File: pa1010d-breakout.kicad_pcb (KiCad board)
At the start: 2 copper layers, 19 x 23 mm, 5 parts, among them J1 Conn_01x08_Male, U1 PA1010D

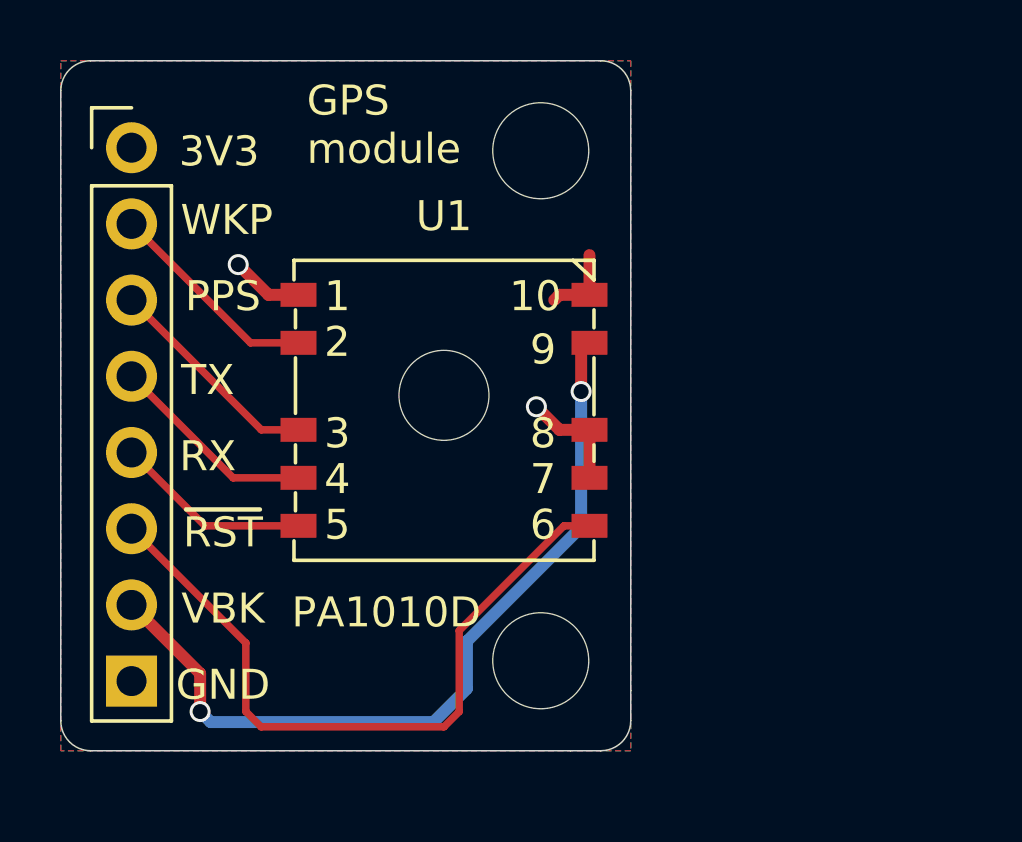
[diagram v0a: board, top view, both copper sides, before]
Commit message: refactor: update schematic according to datasheet V0.3
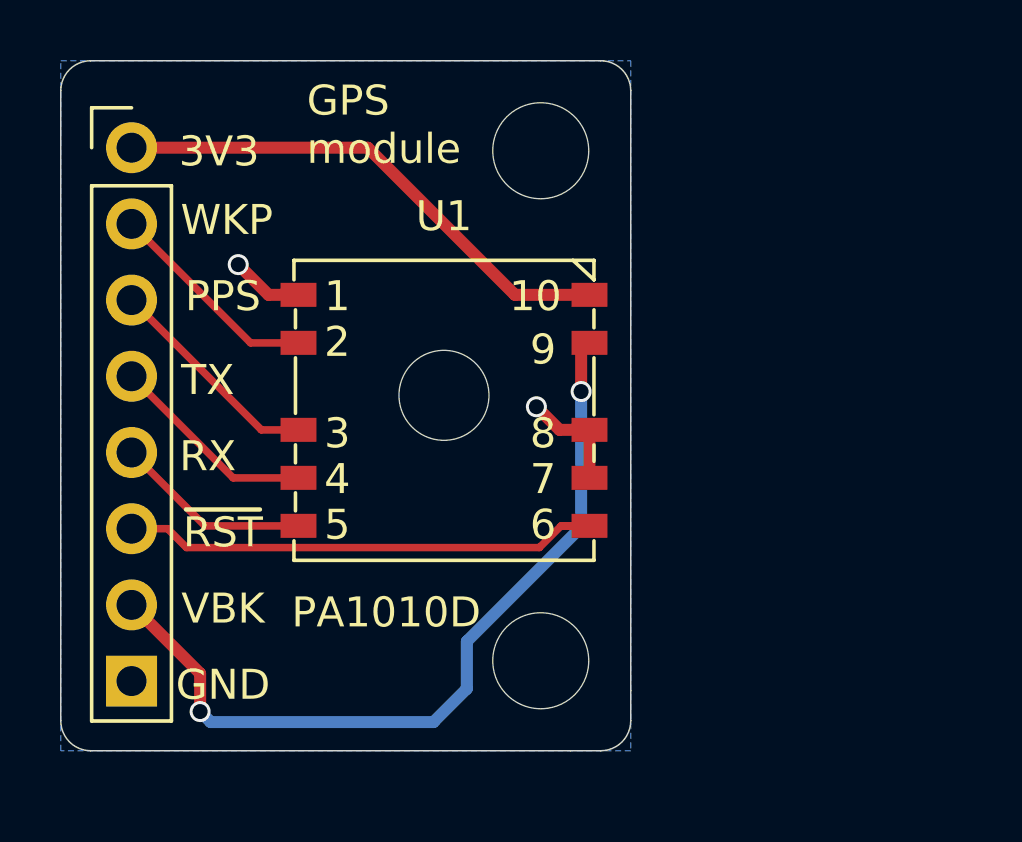
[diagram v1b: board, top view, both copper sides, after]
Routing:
- net +3V3: track 2.57 -> 17.3 mm
- net /NRESET: track 23.7 -> 16.7 mm
- removed copper zone on F.Cu, net +3V3
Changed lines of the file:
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@@
     (thickness 1.6)
     (drawings 52)
-    (tracks 38)
+    (tracks 36)
     (zones 0)
     (modules 5)
@@
   (layers
     (0 F.Cu signal)
-    (31 B.Cu signal)
-    (32 B.Adhes user)
-    (33 F.Adhes user)
-    (34 B.Paste user)
+    (31 B.Cu signal hide)
+    (32 B.Adhes user hide)
+    (33 F.Adhes user hide)
+    (34 B.Paste user hide)
     (35 F.Paste user)
-    (36 B.SilkS user)
+    (36 B.SilkS user hide)
     (37 F.SilkS user)
-    (38 B.Mask user)
+    (38 B.Mask user hide)
     (39 F.Mask user)
-    (40 Dwgs.User user)
-    (41 Cmts.User user)
-    (42 Eco1.User user)
-    (43 Eco2.User user)
+    (40 Dwgs.User user hide)
+    (41 Cmts.User user hide)
+    (42 Eco1.User user hide)
+    (43 Eco2.User user hide)
     (44 Edge.Cuts user)
-    (45 Margin user)
-    (46 B.CrtYd user)
+    (45 Margin user hide)
+    (46 B.CrtYd user hide)
     (47 F.CrtYd user)
-    (48 B.Fab user)
+    (48 B.Fab user hide)
     (49 F.Fab user)
   )
@@
   (segment (start 101.624 82.303) (end 100.624 82.303) (width 0.4) (layer F.Cu) (net 1))
   (via (at 99.855 81.534) (size 0.7) (drill 0.5) (layers F.Cu B.Cu) (net 1))
-  (segment (start 100.624 77.803) (end 100.449 77.978) (width 0.4) (layer F.Cu) (net 2))
-  (segment (start 100.624 77.803) (end 101.624 77.803) (width 0.4) (layer F.Cu) (net 2))
-  (segment (start 101.624 77.803) (end 101.624 76.478) (width 0.4) (layer F.Cu) (net 2))
+  (segment (start 86.36 72.898) (end 94.234 72.898) (width 0.4) (layer F.Cu) (net 2))
+  (segment (start 99.139 77.803) (end 101.624 77.803) (width 0.4) (layer F.Cu) (net 2))
+  (segment (start 94.234 72.898) (end 99.139 77.803) (width 0.4) (layer F.Cu) (net 2))
   (segment (start 86.36 88.138) (end 88.646 90.424) (width 0.4) (layer F.Cu) (net 3))
   (segment (start 88.646 90.424) (end 88.646 91.694) (width 0.4) (layer F.Cu) (net 3))
@@
   (segment (start 97.536 90.932) (end 97.536 89.355998) (width 0.4) (layer B.Cu) (net 3))
   (segment (start 101.346 85.545998) (end 101.346 81.026) (width 0.4) (layer B.Cu) (net 3))
-  (segment (start 97.282 88.995) (end 100.774 85.503) (width 0.25) (layer F.Cu) (net 4))
-  (segment (start 97.282 91.694) (end 97.282 88.995) (width 0.25) (layer F.Cu) (net 4))
   (segment (start 100.774 85.503) (end 101.624 85.503) (width 0.25) (layer F.Cu) (net 4))
-  (segment (start 96.774 92.202) (end 97.282 91.694) (width 0.25) (layer F.Cu) (net 4))
-  (segment (start 90.678 92.202) (end 96.774 92.202) (width 0.25) (layer F.Cu) (net 4))
-  (segment (start 90.17 91.694) (end 90.678 92.202) (width 0.25) (layer F.Cu) (net 4))
-  (segment (start 90.17 89.408) (end 90.17 91.694) (width 0.25) (layer F.Cu) (net 4))
-  (segment (start 86.36 85.598) (end 90.17 89.408) (width 0.25) (layer F.Cu) (net 4))
+  (segment (start 88.192082 86.228001) (end 99.953999 86.228001) (width 0.25) (layer F.Cu) (net 4))
+  (segment (start 87.562081 85.598) (end 88.192082 86.228001) (width 0.25) (layer F.Cu) (net 4))
+  (segment (start 86.36 85.598) (end 87.562081 85.598) (width 0.25) (layer F.Cu) (net 4))
+  (segment (start 100.679 85.503) (end 101.624 85.503) (width 0.25) (layer F.Cu) (net 4))
+  (segment (start 99.953999 86.228001) (end 100.679 85.503) (width 0.25) (layer F.Cu) (net 4))
   (segment (start 88.805 85.503) (end 91.924 85.503) (width 0.25) (layer F.Cu) (net 5))
   (segment (start 86.36 83.058) (end 88.805 85.503) (width 0.25) (layer F.Cu) (net 5))
@@
   (segment (start 90.325 79.403) (end 91.924 79.403) (width 0.25) (layer F.Cu) (net 8))
   (segment (start 86.36 75.438) (end 90.325 79.403) (width 0.25) (layer F.Cu) (net 8))
-  (zone (net 2) (net_name +3V3) (layer F.Cu) (hatch edge 0.508)
-    (connect_pads (clearance 0.508))
-    (min_thickness 0.254)
-    (fill yes (arc_segments 32) (thermal_gap 0.508) (thermal_bridge_width 0.508))
-    (polygon
-      (pts
-        (xy 103 93) (xy 84 93) (xy 84 70) (xy 103 70)
-      )
-    )
-  )
   (zone (net 1) (net_name GND) (layer B.Cu) (hatch edge 0.508)
     (connect_pads (clearance 0.508))

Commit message: refactor: elongate, rotate pads for PA1010D datasheet V0.3
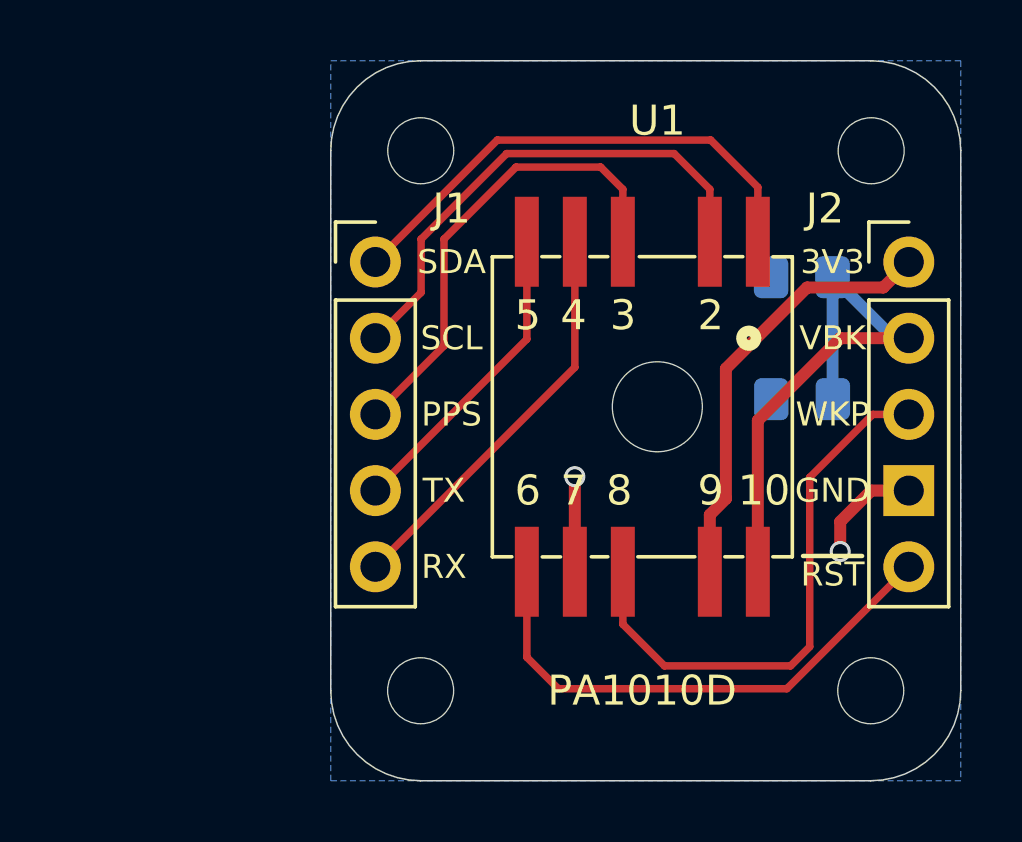
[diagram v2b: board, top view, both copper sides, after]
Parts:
- removed the REF** at (100.0, 73.0)
- removed the REF** at (100.0, 90.0)
- added C1: 0.1uF, Passives:C_0805_2012Metric_Pad1.15x1.40mm_HandSolder, B.Cu at (108.7, 77.2)
- added C2: 1uF, Passives:C_0805_2012Metric_Pad1.15x1.40mm_HandSolder, B.Cu at (108.7, 81.3)
- added J2: Conn_01x05_Male, Connector_PinHeader_2.54mm:PinHeader_1x05_P2.54mm_Vertical, F.Cu at (112.3, 76.7)
- added REF**: MountingHole_2.2mm_M2, MountingHole:MountingHole_2.2mm_M2, F.Cu at (111.0, 91.0)
- added REF**: MountingHole_2.2mm_M2, MountingHole:MountingHole_2.2mm_M2, F.Cu at (96.0, 91.0)
- added REF**: MountingHole_2.2mm_M2, MountingHole:MountingHole_2.2mm_M2, F.Cu at (111.0, 73.0)
- added REF**: MountingHole_2.2mm_M2, MountingHole:MountingHole_2.2mm_M2, F.Cu at (96.0, 73.0)
- J1: value Conn_01x08_Male -> Conn_01x05_Male; footprint Connector_PinHeader_2.54mm:PinHeader_1x08_P2.54mm_Vertical -> Connector_PinHeader_2.54mm:PinHeader_1x05_P2.54mm_Vertical
- moved REF** 9.87 mm to (103.9, 76.7)
- moved J1 8.98 mm to (94.5, 76.7)
- moved U1 7.12 mm to (103.9, 81.5), turned to 270 degrees
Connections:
- J1 pad 1: +3V3 -> /SDA
- J1 pad 2: /WAKEUP -> /SCL
- U1 pad 1: GND -> /SDA
- U1 pad 2: /WAKEUP -> /SCL
- U1 pad 4: /TX -> /RX
- U1 pad 5: /RX -> /TX
- U1 pad 8: GND -> /WAKEUP
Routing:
- net /SCL: track 0.00 -> 17.0 mm
- net /SDA: track 0.00 -> 16.9 mm
- net /VBACKUP: track 27.2 -> 14.6 mm, vias 2 -> 0
- net /WAKEUP: track 7.21 -> 18.6 mm
- net /1PPS: track 7.36 -> 15.8 mm
- net /RX: track 6.58 -> 13.6 mm
- net /TX: track 6.97 -> 10.4 mm
- net +3V3: track 17.3 -> 18.7 mm
- net /NRESET: track 16.7 -> 17.7 mm
- net GND: track 6.11 -> 6.88 mm
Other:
- board size 19 x 23 mm -> 21 x 24 mm
- board text added: "Get started:"
- board text added: "SCL"
- board text added: "SDA"
- board text added: "V2.0 Dec 2019"
- board text added: "hutscape.com/d/pa1010d"
- board text removed: "GPS module"
- board text removed: "V1.0 Nov 2019"
- board text removed: "bit.ly/pa1010d"
